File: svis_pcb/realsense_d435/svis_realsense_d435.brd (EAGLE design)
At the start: 10 parts

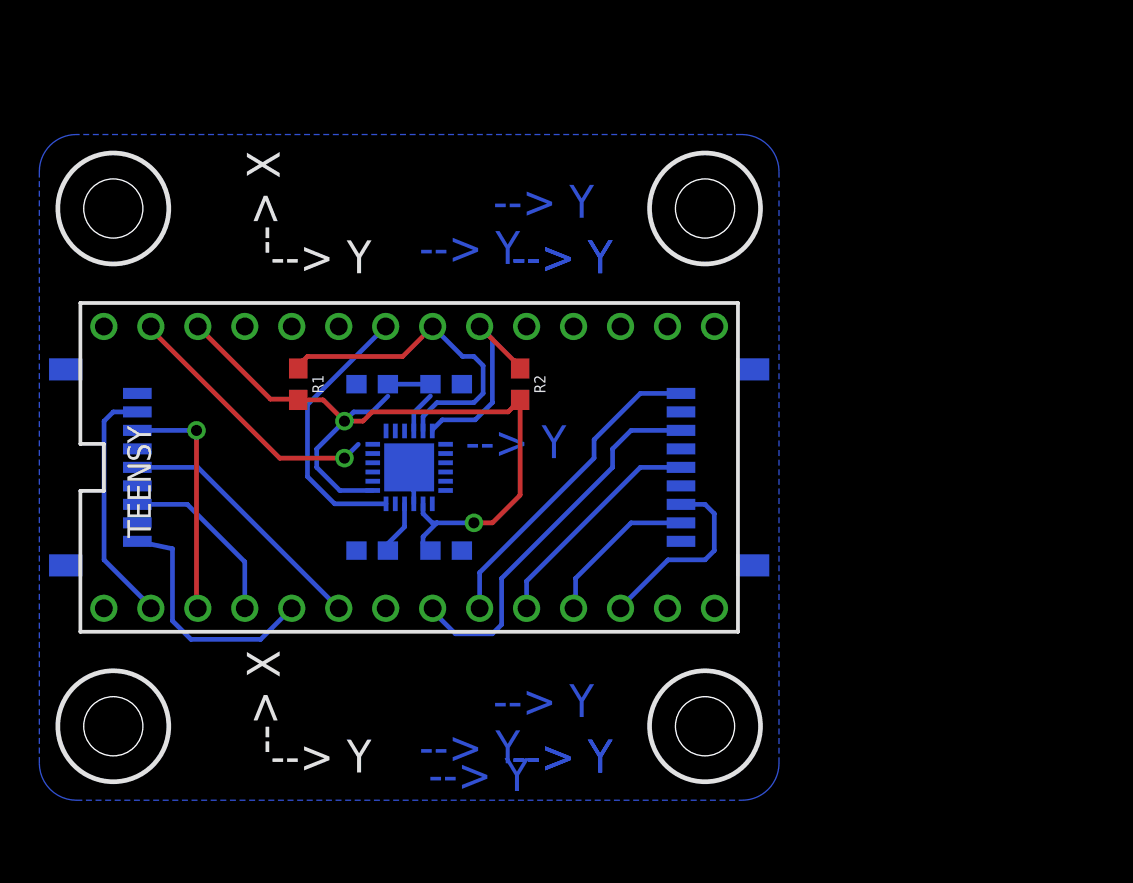
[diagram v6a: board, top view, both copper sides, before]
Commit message: Remove stray trace.
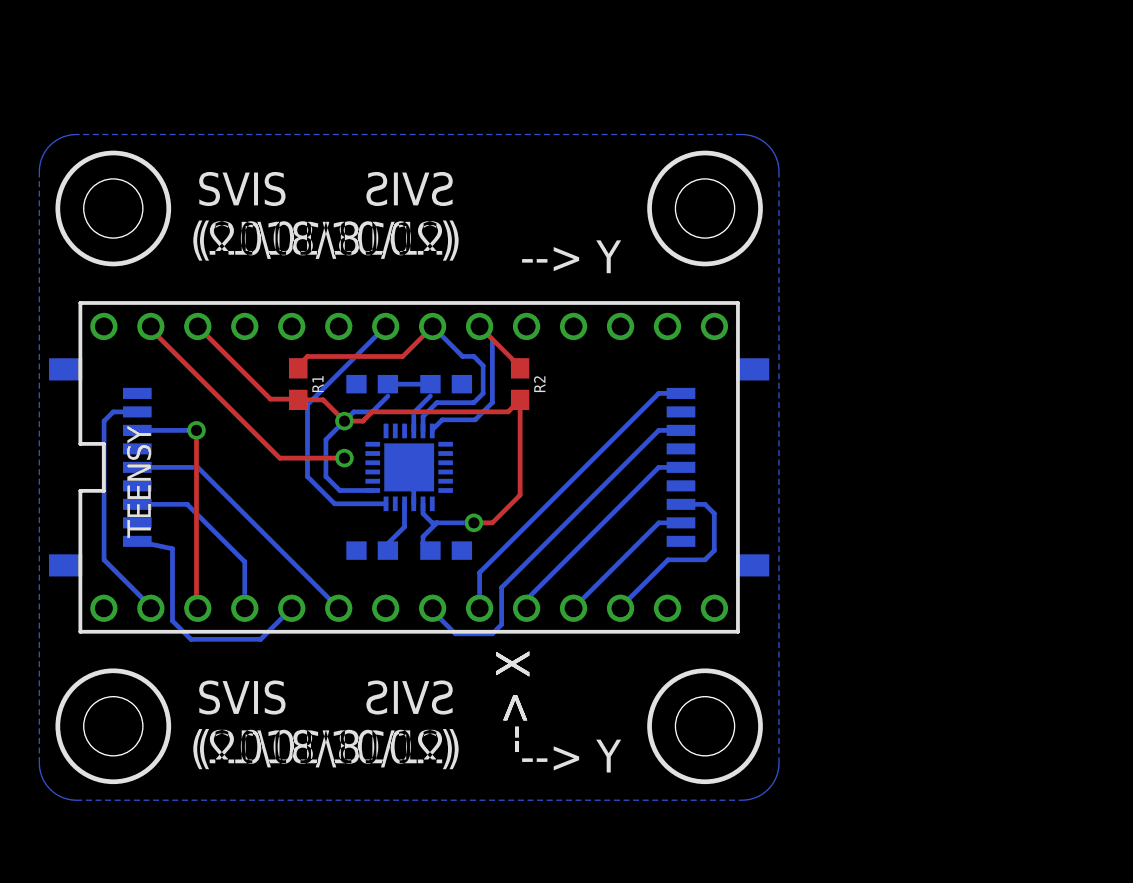
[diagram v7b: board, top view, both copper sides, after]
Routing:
- net GND: track 15.6 -> 14.6 mm
- net CAM2_TRIGGER: track 20.7 -> 19.8 mm
- net CAM2_TX: track 8.61 -> 7.73 mm
- net CAM2_STROBE: track 12.4 -> 11.8 mm
- net CAM2_IO: track 17.4 -> 16.8 mm
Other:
- board text added: "SVIS (2018/10/12)"
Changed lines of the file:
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@@
 <hole x="36" y="4" drill="3.2"/>
 <circle x="36" y="4" radius="3" width="0.254" layer="21"/>
-<text x="31" y="1.5" size="1.778" layer="16" rot="MR0">Y &lt;--</text>
-<text x="31" y="1.5" size="1.778" layer="16" rot="MR0">Y &lt;--</text>
-<text x="28.5" y="18.5" size="1.778" layer="16" rot="MR0">Y &lt;--</text>
-<text x="30" y="4.5" size="1.778" layer="16" rot="MR0">Y &lt;--</text>
-<text x="26" y="2" size="1.778" layer="16" rot="MR0">Y &lt;--</text>
-<text x="26.5" y="0.5" size="1.778" layer="16" rot="MR0">Y &lt;--</text>
 <text x="31.5" y="1.5" size="1.778" layer="26" rot="MR0">Y &lt;--</text>
-<text x="25" y="2.5" size="1.778" layer="26" rot="MR90">--&gt; X</text>
-<text x="31" y="28.5" size="1.778" layer="16" rot="MR0">Y &lt;--</text>
-<text x="31" y="28.5" size="1.778" layer="16" rot="MR0">Y &lt;--</text>
-<text x="30" y="31.5" size="1.778" layer="16" rot="MR0">Y &lt;--</text>
-<text x="26" y="29" size="1.778" layer="16" rot="MR0">Y &lt;--</text>
+<text x="26.5" y="2.5" size="1.778" layer="25" rot="R90">--&gt; X</text>
 <text x="31.5" y="28.5" size="1.778" layer="26" rot="MR0">Y &lt;--</text>
 <text x="25" y="29.5" size="1.778" layer="26" rot="MR90">--&gt; X</text>
-<text x="12.5" y="28.5" size="1.778" layer="25">--&gt; Y</text>
-<text x="12.5" y="1.5" size="1.778" layer="25">--&gt; Y</text>
-<text x="13" y="2.5" size="1.778" layer="25" rot="R90">--&gt; X</text>
-<text x="13" y="29.5" size="1.778" layer="25" rot="R90">--&gt; X</text>
+<text x="26" y="28.5" size="1.778" layer="25">--&gt; Y</text>
+<text x="26" y="1.5" size="1.778" layer="25">--&gt; Y</text>
+<text x="26.5" y="2.5" size="1.778" layer="25" rot="R90">--&gt; X</text>
+<text x="25" y="29.5" size="1.778" layer="26" rot="MR90">--&gt; X</text>
+<text x="22.5" y="2" size="1.778" layer="25" rot="MR0">SVIS
+(2018/10/12)</text>
+<text x="22.5" y="29.5" size="1.778" layer="25" rot="MR0">SVIS
+(2018/10/12)</text>
+<text x="8.5" y="29.5" size="1.778" layer="25">SVIS
+(2018/10/12)</text>
+<text x="8.5" y="2" size="1.778" layer="25">SVIS
+(2018/10/12)</text>
 </plain>
 <attributes>
@@
 <wire x1="20.25" y1="16.75" x2="20" y2="17" width="0.254" layer="16"/>
 <contactref element="ICM20689" pad="25"/>
-<wire x1="17.25" y1="19.25" x2="16.5" y2="18.5" width="0.254" layer="16"/>
+<wire x1="17.25" y1="19.25" x2="16.5" y2="18.5" width="0" layer="19" extent="1-16"/>
 <via x="16.5" y="18.5" extent="1-16" drill="0.6"/>
 <contactref element="ICM20689" pad="18"/>
@@
 <contactref element="ICM20689" pad="13"/>
 <wire x1="18.03" y1="16.75" x2="16.25" y2="16.75" width="0.254" layer="16"/>
-<wire x1="16.25" y1="16.75" x2="15" y2="18" width="0.254" layer="16"/>
-<wire x1="15" y1="19" x2="16.5" y2="20.5" width="0.254" layer="16"/>
-<wire x1="15" y1="19" x2="15" y2="18" width="0.254" layer="16"/>
+<wire x1="16.25" y1="16.75" x2="15.5" y2="17.5" width="0.254" layer="16"/>
+<wire x1="15.5" y1="19.5" x2="16.5" y2="20.5" width="0.254" layer="16"/>
+<wire x1="15.5" y1="19.5" x2="15.5" y2="17.5" width="0.254" layer="16"/>
 <wire x1="18.85" y1="21.85" x2="18.85" y2="22.35" width="0" layer="19" extent="16-16"/>
 <wire x1="21.15" y1="21.86" x2="21.15" y2="22.5" width="0" layer="19" extent="16-16"/>
@@
 <contactref element="CAM2" pad="8"/>
 <contactref element="TEENSY" pad="9"/>
-<wire x1="34.7" y1="15" x2="32" y2="15" width="0.254" layer="16"/>
-<wire x1="32" y1="15" x2="29" y2="12" width="0.254" layer="16"/>
-<wire x1="29" y1="12" x2="29" y2="10.49" width="0.254" layer="16"/>
+<wire x1="34.7" y1="15" x2="33.5" y2="15" width="0.254" layer="16"/>
+<wire x1="33.5" y1="15" x2="29" y2="10.5" width="0.254" layer="16"/>
+<wire x1="29" y1="10.5" x2="29" y2="10.49" width="0.254" layer="16"/>
 <wire x1="29" y1="10.49" x2="28.89" y2="10.38" width="0.254" layer="16"/>
 </signal>
@@
 <wire x1="22.5" y1="9" x2="24.5" y2="9" width="0.254" layer="16"/>
 <wire x1="24.5" y1="9" x2="25" y2="9.5" width="0.254" layer="16"/>
-<wire x1="25" y1="9.5" x2="25" y2="12" width="0.254" layer="16"/>
-<wire x1="25" y1="12" x2="31" y2="18" width="0.254" layer="16"/>
-<wire x1="31" y1="18" x2="31" y2="19" width="0.254" layer="16"/>
-<wire x1="31" y1="19" x2="32" y2="20" width="0.254" layer="16"/>
-<wire x1="32" y1="20" x2="34.7" y2="20" width="0.254" layer="16"/>
+<wire x1="25" y1="9.5" x2="25" y2="11.5" width="0.254" layer="16"/>
+<wire x1="25" y1="11.5" x2="33.5" y2="20" width="0.254" layer="16"/>
+<wire x1="33.5" y1="20" x2="34.7" y2="20" width="0.254" layer="16"/>
 </signal>
 <signal name="CAM2_IO">
@@
 <contactref element="TEENSY" pad="7"/>
 <wire x1="23.81" y1="10.38" x2="23.81" y2="12.31" width="0.254" layer="16"/>
-<wire x1="23.81" y1="12.31" x2="30" y2="18.5" width="0.254" layer="16"/>
-<wire x1="30" y1="18.5" x2="30" y2="19.5" width="0.254" layer="16"/>
-<wire x1="30" y1="19.5" x2="32.5" y2="22" width="0.254" layer="16"/>
-<wire x1="32.5" y1="22" x2="34.7" y2="22" width="0.254" layer="16"/>
+<wire x1="23.81" y1="12.31" x2="33.5" y2="22" width="0.254" layer="16"/>
+<wire x1="33.5" y1="22" x2="34.7" y2="22" width="0.254" layer="16"/>
 </signal>
 <signal name="CAM2_STROBE">
 <contactref element="CAM2" pad="5"/>
 <contactref element="TEENSY" pad="8"/>
-<wire x1="26.35" y1="10.38" x2="26.35" y2="11.85" width="0.254" layer="16"/>
-<wire x1="26.35" y1="11.85" x2="32.5" y2="18" width="0.254" layer="16"/>
-<wire x1="32.5" y1="18" x2="34.7" y2="18" width="0.254" layer="16"/>
+<wire x1="26.35" y1="10.38" x2="26.35" y2="10.85" width="0.254" layer="16"/>
+<wire x1="26.35" y1="10.85" x2="33.5" y2="18" width="0.254" layer="16"/>
+<wire x1="33.5" y1="18" x2="34.7" y2="18" width="0.254" layer="16"/>
 </signal>
 <signal name="N$3">
@@
 </board>
 </drawing>
+<compatibility>
+<note version="6.3" minversion="6.2.2" severity="warning">
+Since Version 6.2.2 text objects can contain more than one line,
+which will not be processed correctly with this version.
+</note>
+</compatibility>
 </eagle>

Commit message: Update board for 10/19/18 V1.4 Oshpark order.
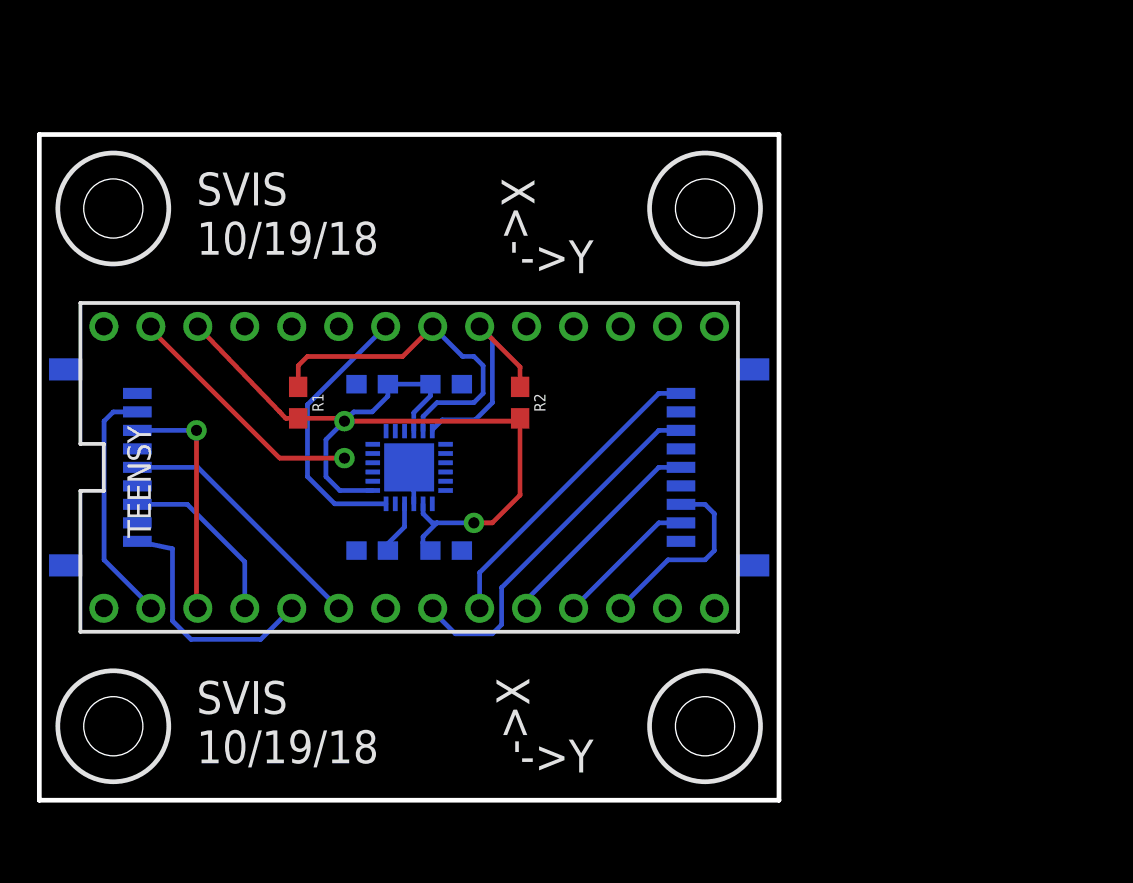
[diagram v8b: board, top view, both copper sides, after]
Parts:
- moved R1 1.00 mm to (14.0, 21.5)
- moved R2 1.00 mm to (26.0, 21.5)
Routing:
- net IMU_SDA: track 11.5 -> 12.5 mm
- net IMU_SCL: track 18.0 -> 19.0 mm
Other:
- board outline added: 40 x 36 mm
- board text added: "->X"
- board text added: "->Y"
- board text added: "SVIS 10/19/18"
- board text added: "Y<-"
- board text removed: "--> X"
- board text removed: "--> Y"
- board text removed: "SVIS (2018/10/12)"
- board text removed: "Y <--"
